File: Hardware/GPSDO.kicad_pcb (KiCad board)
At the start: 2 copper layers, 203.3 x 152.4 mm, 167 parts, among them J201 Line, J202 Earth, J203 Neutral, J204 44472-0453, J301 Ref Divider, J302 Encoder, J303 Ref Select, J304 GPS Module, J305 VCO Range, J306 LCD, J307 Serial, J308 RF 50 Ohm, J309 RF TTL, J310 1PPS TTL, J311 Program, J312 ICSP, J313 USB, J401 OCXO Signal, J402 OCXO Voltage, Q301 2N3904, T201 B82732R2142, T202 FS24-1500, U201 LM7912, U202 LM2596T-5, U203 LM2596T-12, U301 DAC8571IDGK, U302 OP07, U303 OP07, U304 GALI-52, U305 74LVC1G17, U306 74LVC1G17, U307 MAX232, U308 MCP23017_SO, U309 24AA04, U310 PIC18F27Q43, U311 FT232RL, U401 ADCMP600, U402 74LVC1G17, X401 IsoTemp 131, X402 Bliley N47/NV47, X403 IsoTemp 143N, X405 Oscilloquartz 8663, X406 IsoTemp 143A

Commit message: updated pcb
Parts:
- added REF**: MountingHole_3mm_Pad_TopBottom, MountingHole:MountingHole_3mm_Pad_TopBottom, F.Cu at (57.4, 108.2)
- added REF**: MountingHole_3mm_Pad_TopBottom, MountingHole:MountingHole_3mm_Pad_TopBottom, F.Cu at (116.3, 57.4)
- added X404: VECTRON C4550A, DH_OCXO:VectronC4550-A, F.Cu at (74.7, 79.8)
- BT301: value CR2302 -> CR2032
- C313: footprint Capacitor_THT:C_Axial_L3.8mm_D2.6mm_P7.50mm_Horizontal -> Capacitor_SMD:C_0603_1608Metric_Pad1.08x0.95mm_HandSolder
- moved RV301 318.7 mm to (137.7, 69.1)
- moved U309 310.2 mm to (103.1, 123.4)
- moved R305 280.4 mm to (129.0, 105.2)
- moved U308 273.1 mm to (139.8, 90.8)
- moved R307 269.7 mm to (141.2, 106.7)
- moved U310 268.3 mm to (165.4, 70.2)
- moved Q301 259.0 mm to (135.6, 107.7), turned to 90 degrees
- moved BT301 257.0 mm to (121.8, 121.4)
- moved D310 255.1 mm to (114.8, 121.4)
- moved X403 254.8 mm to (86.8, 87.9), turned to 180 degrees
- moved D311 254.7 mm to (114.8, 129.0)
- moved C309 254.6 mm to (190.7, 70.6)
- moved X401 245.5 mm to (90.4, 78.4), turned to 180 degrees
- moved J306 243.3 mm to (128.5, 66.5)
- moved R321 240.4 mm to (197.6, 67.6), turned to 180 degrees
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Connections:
- REF** pad 1: (no net) -> GND (x10)
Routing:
- net GND: track 65.7 -> 314.5 mm, vias 5 -> 10
- net +5V: track 0.00 -> 117.2 mm
- net /Logic/VCO: track 0.00 -> 71.0 mm
- net /Logic/VRef: track 0.00 -> 64.9 mm
- net /Power Supply/Neutral_Filter_2: track 147.5 -> 93.1 mm
- net /Power Supply/Reg_5_FB: track 0.00 -> 46.5 mm
- net -12V: track 0.00 -> 46.2 mm
- net Net-(J402-Pin_2): track 0.00 -> 42.6 mm
- net +12V: track 0.00 -> 42.2 mm
- net Net-(X401-RF_Out): track 0.00 -> 38.2 mm
- net /Power Supply/Reg_Pos_5_Out: track 0.00 -> 32.6 mm, vias 0 -> 1
- net /OCXO/OCXO_Signal: track 0.00 -> 32.6 mm
- net /Logic/LCD_BL: track 0.00 -> 25.3 mm
- net /Logic/TXD: track 0.00 -> 23.4 mm
- net /Logic/RS232_C1-: track 0.00 -> 20.1 mm
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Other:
- board text added: "Caution: Heat sinks are grounded!"
- board text added: "Caution: Line voltages present in this box:"
- board text added: "Fault"
- board text added: "GPS"
- board text added: "Hold"
- board text added: "Insulate above and below with foam!"
- board text added: "LCD Contrast"
- board text added: "Lock"
- board text added: "Power"
- board text added: "USB RX"
- board text added: "USB TX"

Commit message: Updated PCB
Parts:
- C304: value 0.1 -> 100n
- moved J402 177.1 mm to (101.5, 117.0), turned to 90 degrees
- moved J311 168.8 mm to (152.0, 68.6), turned to -90 degrees
- moved TP305 167.9 mm to (142.6, 70.0)
- moved J312 165.8 mm to (150.8, 77.1), turned to 90 degrees
- moved C401 154.0 mm to (133.5, 58.4)
- moved J401 150.6 mm to (128.0, 54.6)
- moved R322 149.1 mm to (142.4, 104.1)
- moved R406 141.2 mm to (133.5, 53.9)
- moved R323 140.8 mm to (151.9, 104.3), turned to 180 degrees
- moved D402 136.2 mm to (137.7, 58.5)
- moved U401 134.7 mm to (151.8, 62.6)
- moved J302 134.2 mm to (169.8, 94.5), turned to 180 degrees
- moved D401 134.2 mm to (137.7, 63.0), turned to 180 degrees
- moved R401 133.4 mm to (133.6, 63.0)
- moved R402 127.3 mm to (142.1, 58.5), turned to 90 degrees
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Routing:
- net /Logic/VCO: track 71.0 -> 251.3 mm
- net /Logic/LED_Fault: track 0.00 -> 129.0 mm
- net /Logic/LED_Power: track 0.00 -> 122.7 mm
- net /Logic/LED_LOCK_N: track 0.00 -> 116.6 mm
- net /Logic/LED_HOLDOVER_N: track 0.00 -> 110.6 mm
- net /Logic/LED_GPS_N: track 0.00 -> 104.4 mm
- net Net-(U311-CBUS0): track 0.00 -> 85.5 mm
- net Net-(U311-CBUS1): track 0.00 -> 85.1 mm
- net /Logic/SDA: track 0.00 -> 83.9 mm, vias 0 -> 3
- net /Logic/GPS_TX: track 0.00 -> 80.6 mm, vias 0 -> 1
- net /Logic/GPS_RX: track 0.00 -> 76.4 mm, vias 0 -> 1
- net /Logic/SCL: track 0.00 -> 75.5 mm, vias 0 -> 3
- net /OCXO/OCXO_Signal: track 32.6 -> 92.8 mm
- net GND: track 314.5 -> 356.1 mm, vias 10 -> 39
- net /Logic/USB_TX: track 0.00 -> 39.0 mm, vias 0 -> 2
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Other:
- board text added: "+12"
- board text added: "+5"
- board text added: "X1"
- board text added: "X2"

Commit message: updated pcb
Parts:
- removed J301: Ref Divider, Connector_PinHeader_2.54mm:PinHeader_2x02_P2.54mm_Vertical
- added ?: , , F.Cu at (163.8, 101.7)
- added ?: , , F.Cu at (165.3, 88.5)
- added ?: , , F.Cu at (167.2, 101.8)
- added ?: , , F.Cu at (163.8, 92.2)
- added J314: Ref Select, Connector_PinHeader_2.54mm:PinHeader_1x03_P2.54mm_Vertical, F.Cu at (180.7, 96.0)
- J303: footprint Connector_PinHeader_2.54mm:PinHeader_1x02_P2.54mm_Vertical -> Connector_PinHeader_2.54mm:PinHeader_1x03_P2.54mm_Vertical
- moved C312 95.2 mm to (179.0, 89.3)
- moved C311 93.4 mm to (178.8, 81.0)
- moved TP301 74.2 mm to (196.2, 106.9)
- moved TP304 63.2 mm to (205.0, 108.3)
- moved TP303 47.9 mm to (221.9, 109.1)
- moved TP302 40.3 mm to (226.9, 88.6)
- moved U301 9.84 mm to (189.6, 91.1), turned to 180 degrees
- moved J303 2.95 mm to (198.2, 100.6), turned to 180 degrees
- turned R301 to 180 degrees
- turned R302 to 180 degrees
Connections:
- U307 pad 11: /Logic/EXT_TX -> Net-(JP301-A)
- U307 pad 12: /Logic/EXT_RX -> Net-(JP302-A)
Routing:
- net +5V: track 150.3 -> 752.2 mm, vias 15 -> 24
- net +12V: track 61.1 -> 356.7 mm, vias 2 -> 8
- net /Logic/RF: track 0.00 -> 179.9 mm, vias 0 -> 4
- net -12V: track 47.9 -> 225.8 mm, vias 1 -> 6
- net /Logic/1PPS: track 0.00 -> 142.7 mm, vias 0 -> 1
- net /Logic/VRef: track 64.9 -> 197.6 mm, vias 0 -> 1
- net /Logic/Int_Ref: track 0.00 -> 65.6 mm, vias 0 -> 2
- net GND: track 356.1 -> 410.2 mm, vias 39 -> 41
- net /Logic/SCL: track 75.5 -> 118.6 mm, vias 3 -> 4
- net /Logic/SDA: track 83.9 -> 126.9 mm, vias 3 -> 4
- net Net-(J303-Pin_2): track 0.00 -> 26.8 mm
- net Net-(J314-Pin_1): track 0.00 -> 18.8 mm
- net /Logic/VCO: track 251.3 -> 266.5 mm
- net /Logic/VRef_FB: track 0.00 -> 11.8 mm
- net Net-(JP301-A): track 0.00 -> 8.79 mm
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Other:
- board text added: "Internal"
- board text added: "JP301"
- board text added: "JP302"
- board text added: "OCXO"

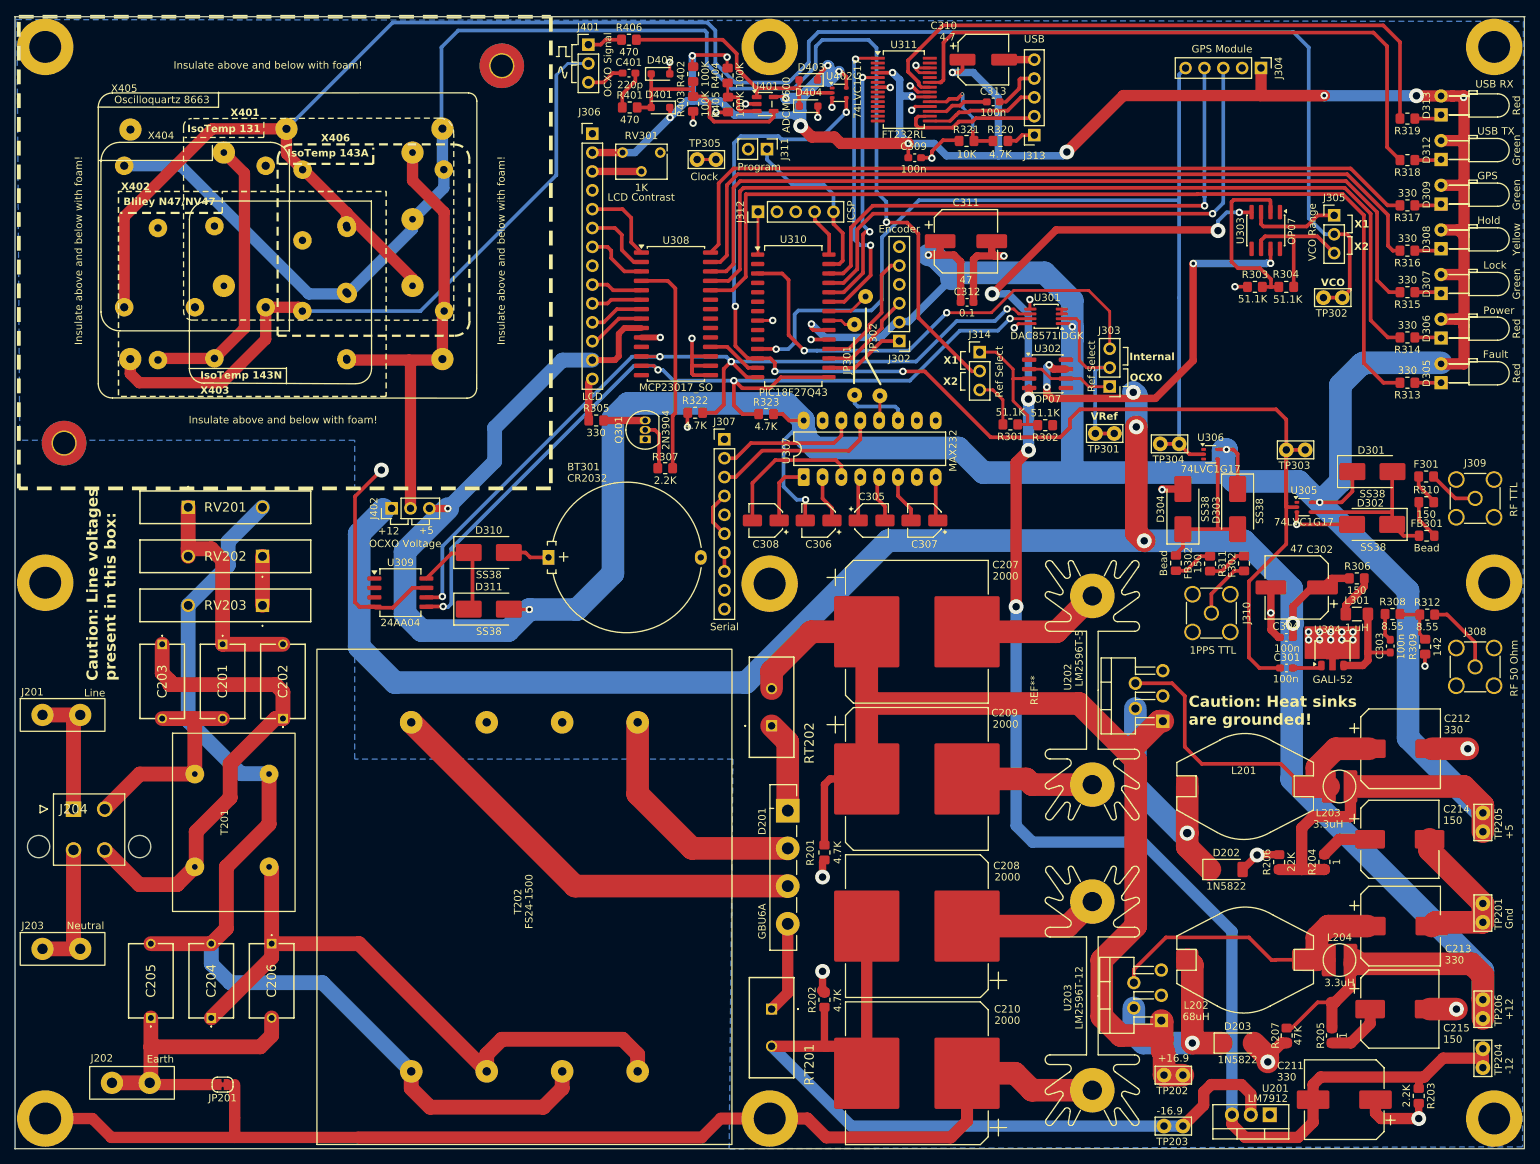
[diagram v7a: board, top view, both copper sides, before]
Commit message: Updated PCB; ran DRC; fixing errors
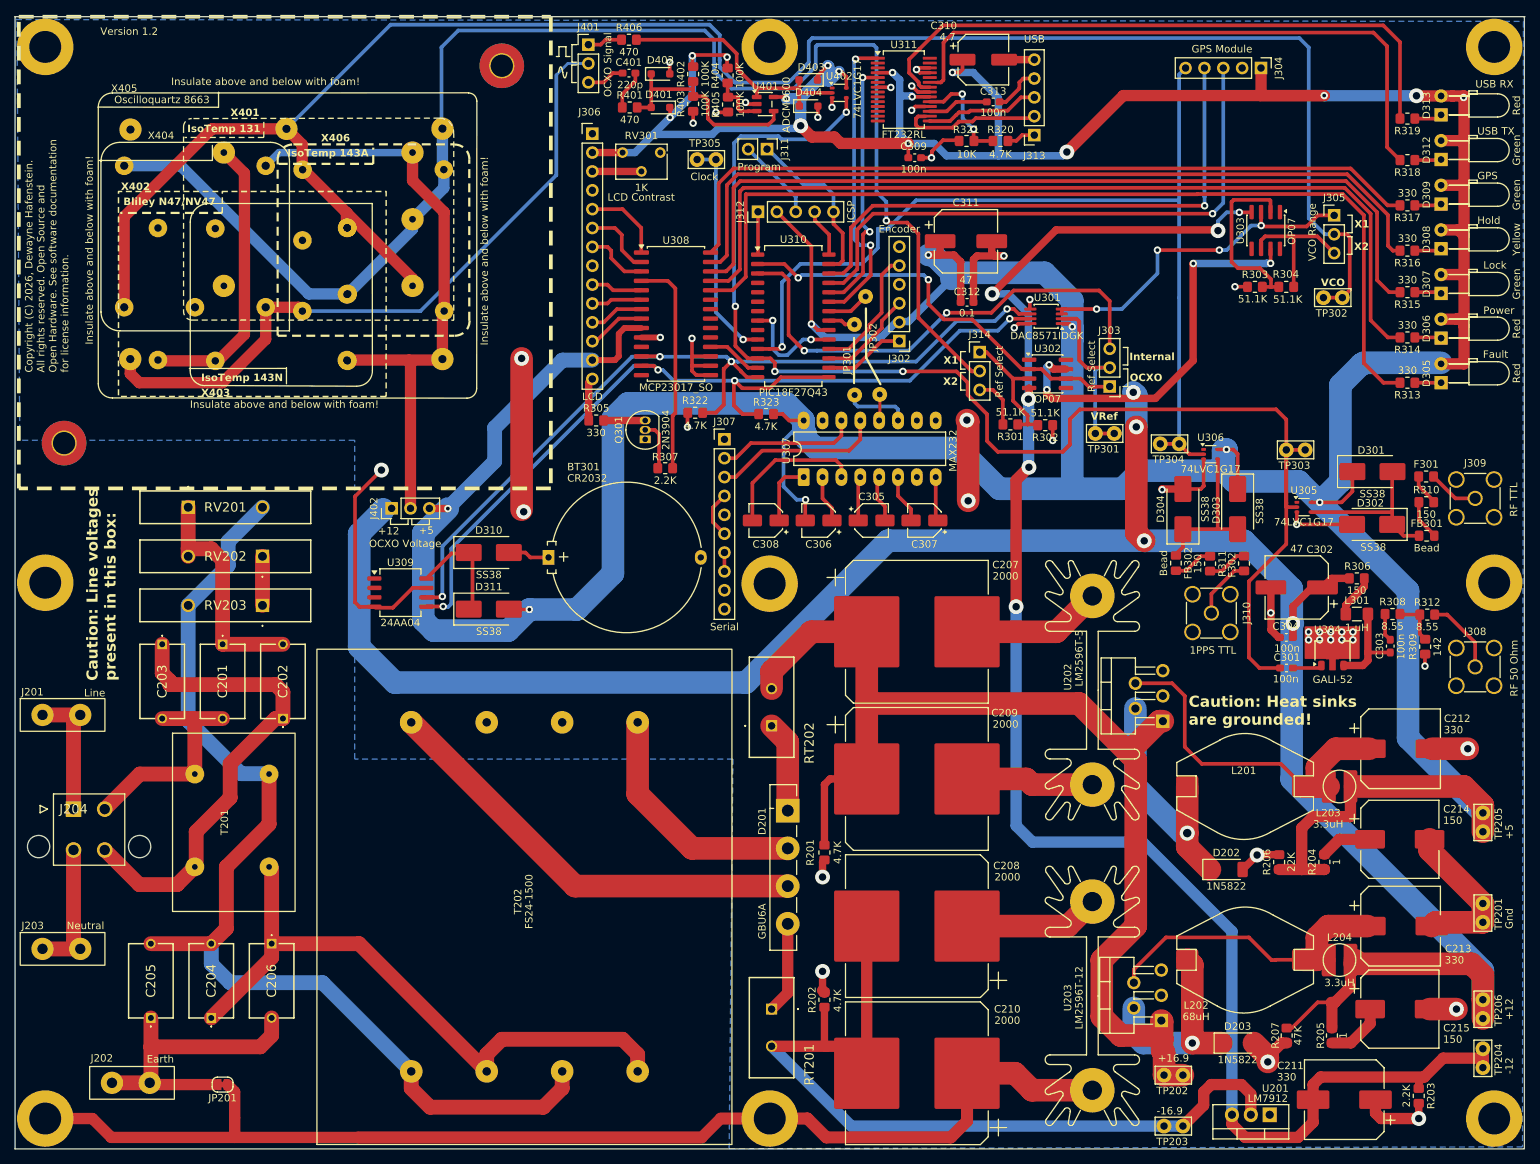
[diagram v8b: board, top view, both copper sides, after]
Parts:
- moved X403 0.35 mm to (86.9, 88.2)
- moved ? 0.18 mm to (167.2, 101.7)
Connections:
- REF** pad 1: GND -> (no net)
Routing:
- net GND: track 410.2 -> 465.4 mm, vias 41 -> 46
- net /Logic/VRef_FB: track 11.8 -> 56.4 mm, vias 0 -> 2
- net Net-(J305-Pin_1): track 12.9 -> 46.3 mm, vias 0 -> 4
- net Net-(U310-RA6): track 2.54 -> 30.2 mm, vias 0 -> 1
- net +5V: track 752.2 -> 773.9 mm
- net Net-(J402-Pin_2): track 62.7 -> 83.2 mm
- net /Logic/RF: track 179.9 -> 185.9 mm
- net Net-(J303-Pin_2): track 26.8 -> 25.1 mm
- net Net-(U311-CBUS0): track 84.1 -> 83.1 mm
- net Net-(J314-Pin_1): track 18.8 -> 17.8 mm
- net /Logic/VCO: track 266.5 -> 265.6 mm
- net /Logic/VRef: track 197.6 -> 196.7 mm
- net /Logic/Int_Ref: track 65.6 -> 66.4 mm
- net /Logic/PGC: track 23.8 -> 22.9 mm
- net Net-(U311-3V3OUT): track 7.45 -> 8.20 mm
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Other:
- board text added: "Copyright (C) 2026, Dewayne Hafenstein. All rights reserved. Open Source and Open Hardware. See software documentation for license information."
- board text added: "Version 1.2"
